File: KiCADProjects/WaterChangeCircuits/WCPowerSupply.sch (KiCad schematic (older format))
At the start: 3 parts, among them J54 Barrel_Jack, J55 Conn_02x02_Odd_Even, J56 Conn_01x02

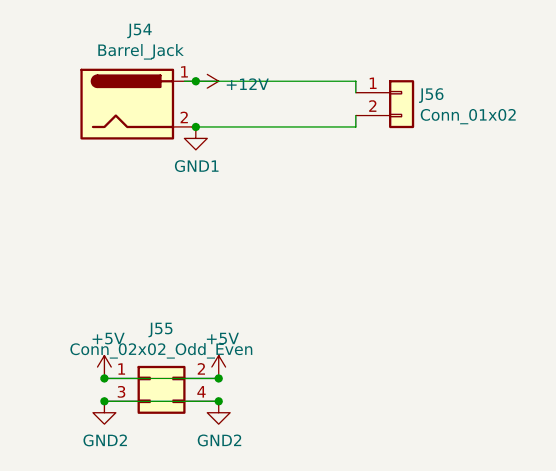
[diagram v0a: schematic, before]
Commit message: Completed PCB design and schematics.
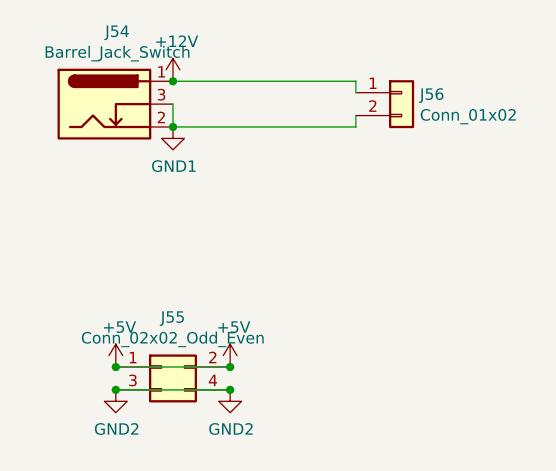
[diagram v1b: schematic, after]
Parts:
- removed J54: Barrel_Jack, Connector_BarrelJack:BarrelJack_CUI_PJ-102AH_Horizontal, symbol Connector:Barrel_Jack
- added J54: Barrel_Jack_Switch, Connector_BarrelJack:BarrelJack_CUI_PJ-102AH_Horizontal, symbol Connector:Barrel_Jack_Switch
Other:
- moved on the sheet: J55
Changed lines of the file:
@@
 $EndDescr
-$Comp
-L Connector:Barrel_Jack J54
-U 1 1 60F2C733
-P 1700 1300
-F 0 "J54" H 1757 1625 50  0000 C CNN
-F 1 "Barrel_Jack" H 1757 1534 50  0000 C CNN
-F 2 "Connector_BarrelJack:BarrelJack_CUI_PJ-102AH_Horizontal" H 1750 1260 50  0001 C CNN
-F 3 "~" H 1750 1260 50  0001 C CNN
-	1    1700 1300
-	1    0    0    -1
-$EndComp
-$Comp
-L power:+12V #PWR0152
-U 1 1 60F2CBF4
-P 2000 1200
-F 0 "#PWR0152" H 2000 1050 50  0001 C CNN
-F 1 "+12V" V 2015 1328 50  0000 L CNN
-F 2 "" H 2000 1200 50  0001 C CNN
-F 3 "" H 2000 1200 50  0001 C CNN
-	1    2000 1200
-	0    1    1    0
-$EndComp
-$Comp
-L power:GND1 #PWR0153
-U 1 1 60F2CE88
-P 2000 1400
-F 0 "#PWR0153" H 2000 1150 50  0001 C CNN
-F 1 "GND1" H 2005 1227 50  0000 C CNN
-F 2 "" H 2000 1400 50  0001 C CNN
-F 3 "" H 2000 1400 50  0001 C CNN
-	1    2000 1400
-	1    0    0    -1
-$EndComp
 $Comp
 L Connector_Generic:Conn_02x02_Odd_Even J55
 U 1 1 60F2DCF3
-P 1800 2500
-F 0 "J55" H 1850 2717 50  0000 C CNN
-F 1 "Conn_02x02_Odd_Even" H 1850 2626 50  0000 C CNN
-F 2 "Connector_PinHeader_2.54mm:PinHeader_2x02_P2.54mm_Vertical" H 1800 2500 50  0001 C CNN
-F 3 "~" H 1800 2500 50  0001 C CNN
-	1    1800 2500
+P 1850 2450
+F 0 "J55" H 1900 2667 50  0000 C CNN
+F 1 "Conn_02x02_Odd_Even" H 1900 2576 50  0000 C CNN
+F 2 "Connector_PinHeader_2.54mm:PinHeader_2x02_P2.54mm_Vertical" H 1850 2450 50  0001 C CNN
+F 3 "~" H 1850 2450 50  0001 C CNN
+	1    1850 2450
 	1    0    0    -1
 $EndComp
@@
 L power:+5V #PWR0150
 U 1 1 60F2EEF2
-P 1600 2500
-F 0 "#PWR0150" H 1600 2350 50  0001 C CNN
-F 1 "+5V" H 1615 2673 50  0000 C CNN
-F 2 "" H 1600 2500 50  0001 C CNN
-F 3 "" H 1600 2500 50  0001 C CNN
-	1    1600 2500
+P 1650 2450
+F 0 "#PWR0150" H 1650 2300 50  0001 C CNN
+F 1 "+5V" H 1665 2623 50  0000 C CNN
+F 2 "" H 1650 2450 50  0001 C CNN
+F 3 "" H 1650 2450 50  0001 C CNN
+	1    1650 2450
 	1    0    0    -1
 $EndComp
@@
 L power:GND2 #PWR0151
 U 1 1 60F2F2C9
-P 1600 2600
-F 0 "#PWR0151" H 1600 2350 50  0001 C CNN
-F 1 "GND2" H 1605 2427 50  0000 C CNN
-F 2 "" H 1600 2600 50  0001 C CNN
-F 3 "" H 1600 2600 50  0001 C CNN
-	1    1600 2600
+P 1650 2550
+F 0 "#PWR0151" H 1650 2300 50  0001 C CNN
+F 1 "GND2" H 1655 2377 50  0000 C CNN
+F 2 "" H 1650 2550 50  0001 C CNN
+F 3 "" H 1650 2550 50  0001 C CNN
+	1    1650 2550
 	1    0    0    -1
 $EndComp
 Wire Wire Line
-	1600 2500 2100 2500
-Connection ~ 1600 2500
+	1650 2450 2150 2450
+Connection ~ 1650 2450
 Wire Wire Line
-	1600 2600 2100 2600
-Connection ~ 1600 2600
+	1650 2550 2150 2550
+Connection ~ 1650 2550
 $Comp
 L power:+5V #PWR0154
 U 1 1 60F2F8BF
-P 2100 2500
-F 0 "#PWR0154" H 2100 2350 50  0001 C CNN
-F 1 "+5V" H 2115 2673 50  0000 C CNN
-F 2 "" H 2100 2500 50  0001 C CNN
-F 3 "" H 2100 2500 50  0001 C CNN
-	1    2100 2500
+P 2150 2450
+F 0 "#PWR0154" H 2150 2300 50  0001 C CNN
+F 1 "+5V" H 2165 2623 50  0000 C CNN
+F 2 "" H 2150 2450 50  0001 C CNN
+F 3 "" H 2150 2450 50  0001 C CNN
+	1    2150 2450
 	1    0    0    -1
 $EndComp
-Connection ~ 2100 2500
+Connection ~ 2150 2450
 $Comp
 L power:GND2 #PWR0155
 U 1 1 60F2FC4F
-P 2100 2600
-F 0 "#PWR0155" H 2100 2350 50  0001 C CNN
-F 1 "GND2" H 2105 2427 50  0000 C CNN
-F 2 "" H 2100 2600 50  0001 C CNN
-F 3 "" H 2100 2600 50  0001 C CNN
-	1    2100 2600
+P 2150 2550
+F 0 "#PWR0155" H 2150 2300 50  0001 C CNN
+F 1 "GND2" H 2155 2377 50  0000 C CNN
+F 2 "" H 2150 2550 50  0001 C CNN
+F 3 "" H 2150 2550 50  0001 C CNN
+	1    2150 2550
 	1    0    0    -1
 $EndComp
-Connection ~ 2100 2600
+Connection ~ 2150 2550
 $Comp
 L Connector_Generic:Conn_01x02 J56
@@
 	1    0    0    -1
 $EndComp
+$Comp
+L Connector:Barrel_Jack_Switch J54
+U 1 1 6102AE3F
+P 1600 1300
+F 0 "J54" H 1657 1617 50  0000 C CNN
+F 1 "Barrel_Jack_Switch" H 1657 1526 50  0000 C CNN
+F 2 "Connector_BarrelJack:BarrelJack_CUI_PJ-102AH_Horizontal" H 1650 1260 50  0001 C CNN
+F 3 "~" H 1650 1260 50  0001 C CNN
+	1    1600 1300
+	1    0    0    -1
+$EndComp
+$Comp
+L power:+12V #PWR06
+U 1 1 6102B742
+P 1900 1200
+F 0 "#PWR06" H 1900 1050 50  0001 C CNN
+F 1 "+12V" H 1915 1373 50  0000 C CNN
+F 2 "" H 1900 1200 50  0001 C CNN
+F 3 "" H 1900 1200 50  0001 C CNN
+	1    1900 1200
+	1    0    0    -1
+$EndComp
+$Comp
+L power:GND1 #PWR07
+U 1 1 6102BB60
+P 1900 1400
+F 0 "#PWR07" H 1900 1150 50  0001 C CNN
+F 1 "GND1" H 1905 1227 50  0000 C CNN
+F 2 "" H 1900 1400 50  0001 C CNN
+F 3 "" H 1900 1400 50  0001 C CNN
+	1    1900 1400
+	1    0    0    -1
+$EndComp
 Wire Wire Line
-	1950 1200 2000 1200
+	1900 1300 1900 1400
+Connection ~ 1900 1400
+Wire Wire Line
+	1900 1200 2700 1200
 Wire Wire Line
 	2700 1200 2700 1250
-Connection ~ 2000 1200
+Connection ~ 1900 1200
 Wire Wire Line
-	2000 1200 2700 1200
-Wire Wire Line
-	2000 1400 2700 1400
+	1900 1400 2700 1400
 Wire Wire Line
 	2700 1400 2700 1350
-Connection ~ 2000 1400
 $EndSCHEMATC
